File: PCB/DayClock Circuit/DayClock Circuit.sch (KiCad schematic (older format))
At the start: 28 parts, among them J10 Conn_02x08_Odd_Even, J11 Conn_01x02, J3 molex 15-24-4441, J5 4002 LCD Screen, J6 Encoder, J7 RGB_LED_Strip_Connector, J8 RGB_LED_Strip_Connector, J9 RGB_LED_Strip_Connector, Q1 N-MOSFET, Q2 N-MOSFET, Q3 N-MOSFET, Q4 N-MOSFET, Q5 N-MOSFET, Q6 N-MOSFET, Q7 N-MOSFET, Q8 N-MOSFET, Q9 N-MOSFET, U1 Tiny_RTC_DS1307

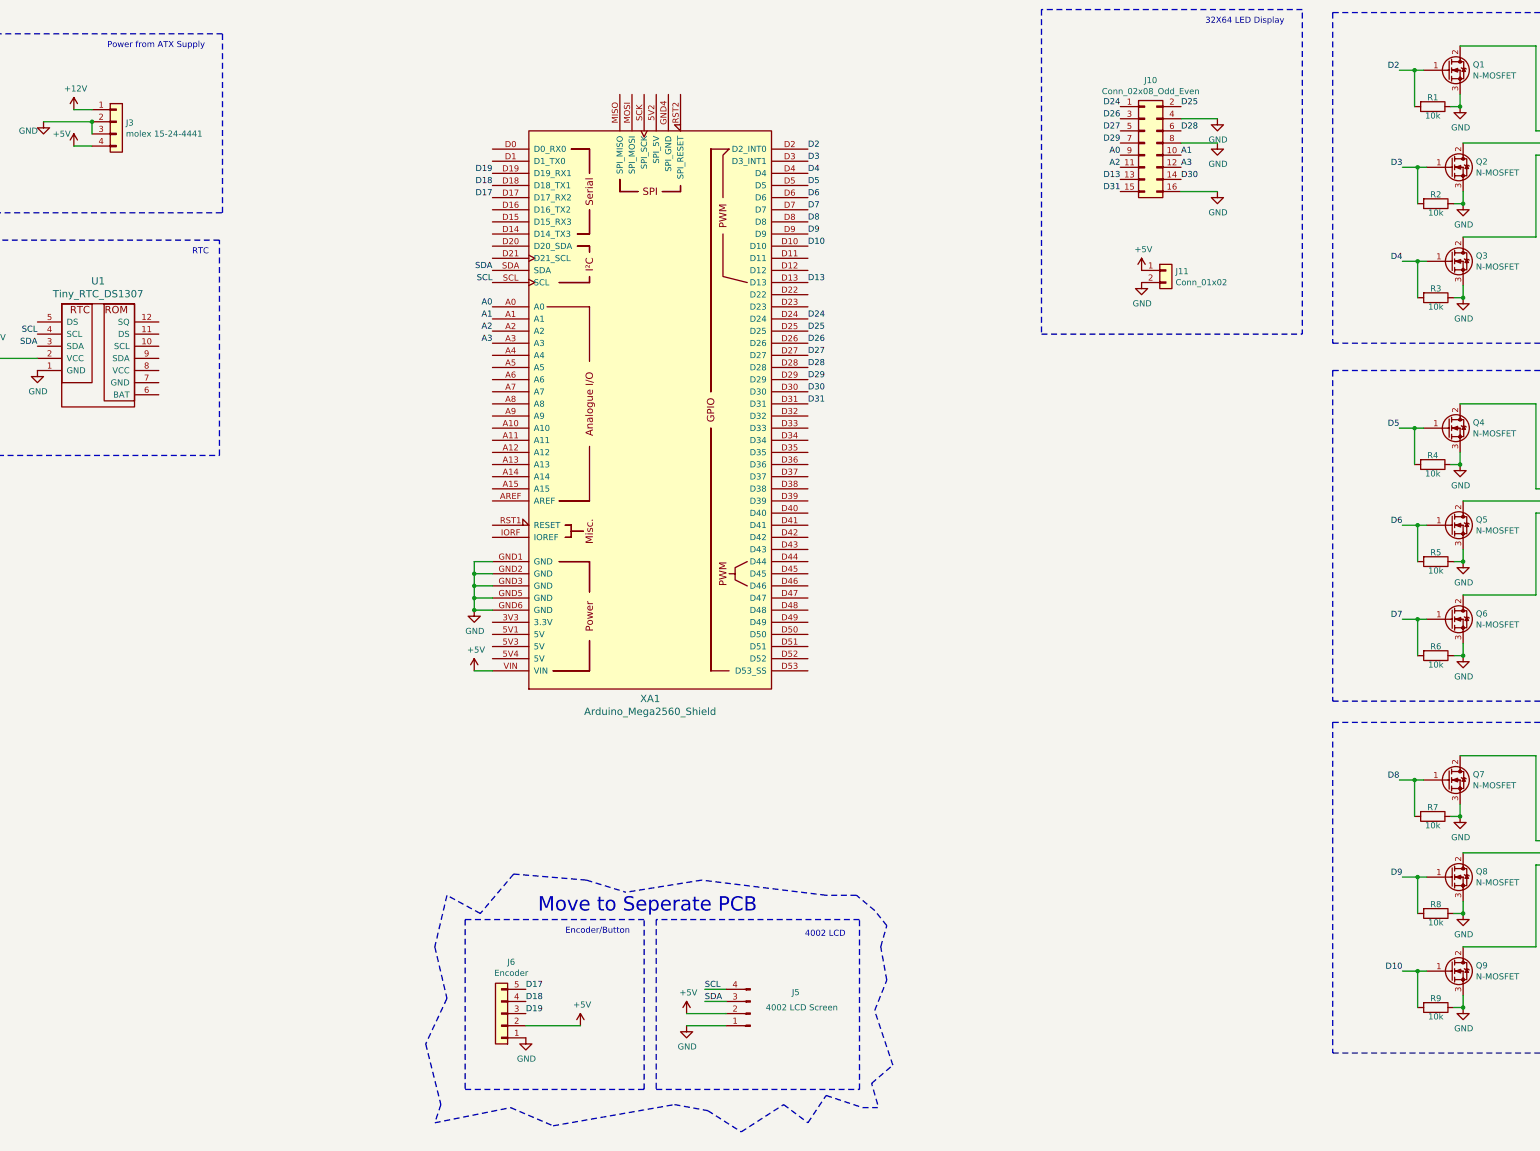
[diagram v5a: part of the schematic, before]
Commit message: Added Stepper with Driver and Proximity Sensor Limits
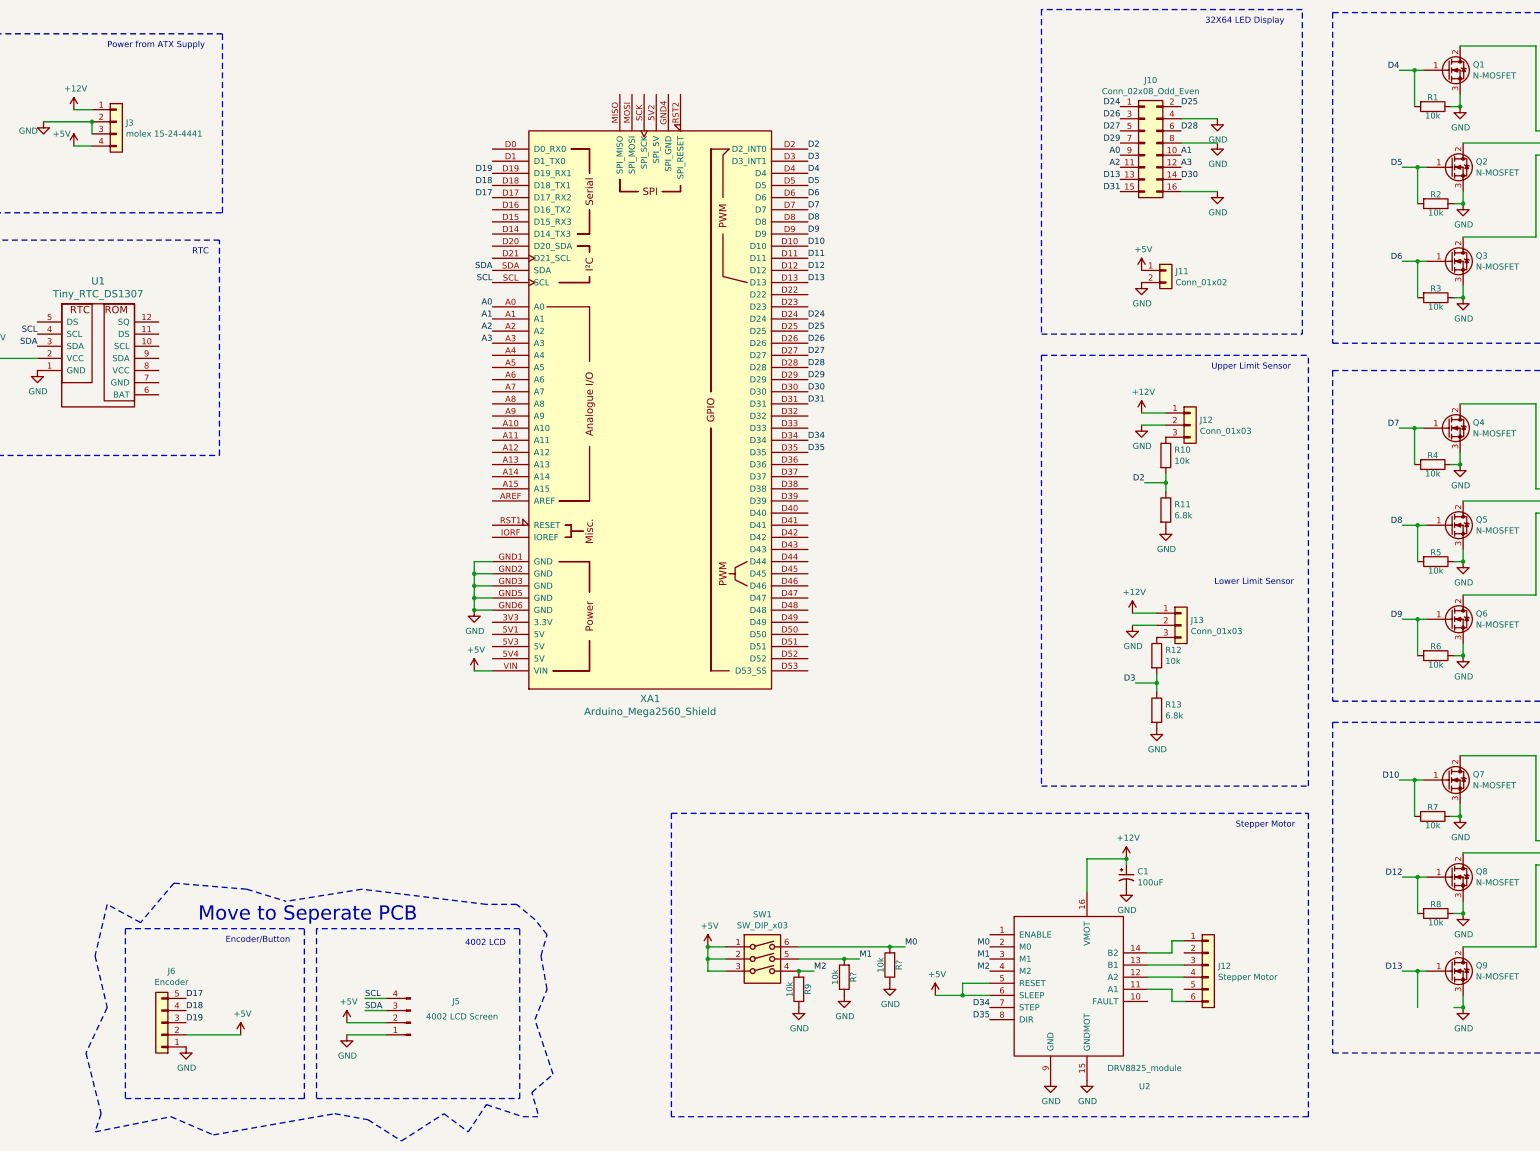
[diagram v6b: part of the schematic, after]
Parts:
- added C1: 100uF, symbol Device:CP1_Small
- added J12, J13: Conn_01x03, Connector_JST:JST_XH_B03B-XH-A_1x03_P2.50mm_Vertical, symbol Connector_Generic:Conn_01x03
- added J12: Stepper Motor, symbol Connector_Generic:Conn_01x06
- added R10, R12, R? (x2): 10k, Resistor_SMD:R_0805_2012Metric_Pad1.15x1.50mm_HandSolder, symbol Device:R
- added R11, R13: 6.8k, Resistor_SMD:R_0805_2012Metric_Pad1.15x1.50mm_HandSolder, symbol Device:R
- added SW1: SW_DIP_x03, symbol Switch:SW_DIP_x03
- added U2: DRV8825_module, symbol rich_symbols:DRV8825_module
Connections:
- net +12V: now also C1.1, J12.1 (Pin_1), J13.1 (Pin_1), U2.16 (VMOT)
- net +5V: now also SW1.1, SW1.2, SW1.3, U2.5 (RESET), U2.6 (SLEEP)
- net D10: now also Q7.1 (G), R7.2; no longer Q9.1 (G), R9.2
- net D13: now also Q9.1 (G)
- net D2: now also R10.2, R11.1; no longer Q1.1 (G), R1.2
- net D3: now also R12.2, R13.1; no longer Q2.1 (G), R2.2
- net D4: now also Q1.1 (G), R1.2; no longer Q3.1 (G), R3.2
- net D5: now also Q2.1 (G), R2.2; no longer Q4.1 (G), R4.2
- net D6: now also Q3.1 (G), R3.2; no longer Q5.1 (G), R5.2
- net D7: now also Q4.1 (G), R4.2; no longer Q6.1 (G), R6.2
- net D8: now also Q5.1 (G), R5.2; no longer Q7.1 (G), R7.2
- net D9: now also Q6.1 (G), R6.2; no longer Q8.1 (G), R8.2
- net GND: now also C1.2, J12.2 (Pin_2), J13.2 (Pin_2), R11.2, R13.2, R?.1, R?.1, U2.15 (GNDMOT), U2.9 (GND)
- net D11: now reaches XA1.D11
- net D12: now reaches XA1.D12
- net D12: now also Q8.1 (G), R8.2
- net D34: now reaches XA1.D34
- net D34: now also U2.7 (STEP)
- net D35: now reaches XA1.D35
- net D35: now also U2.8 (DIR)
- new net: J12.3 (Pin_3), R10.1
- new net: J13.3 (Pin_3), R12.1
- new net: J12.6 (Pin_6), U2.11 (A1)
- new net: J12.4 (Pin_4), U2.12 (A2)
- new net: J12.3 (Pin_3), U2.13 (B1)
- new net: J12.1 (Pin_1), U2.14 (B2)
- new net M0: R?.2, SW1.6, U2.2 (M0)
- new net M1: R?.2, SW1.5, U2.3 (M1)
- new net M2: R9.2, SW1.4, U2.4 (M2)
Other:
- note added: "Lower Limit Sensor"
- note added: "Stepper Motor"
- note added: "Upper Limit Sensor"
- moved on the sheet: J5, J6, R9

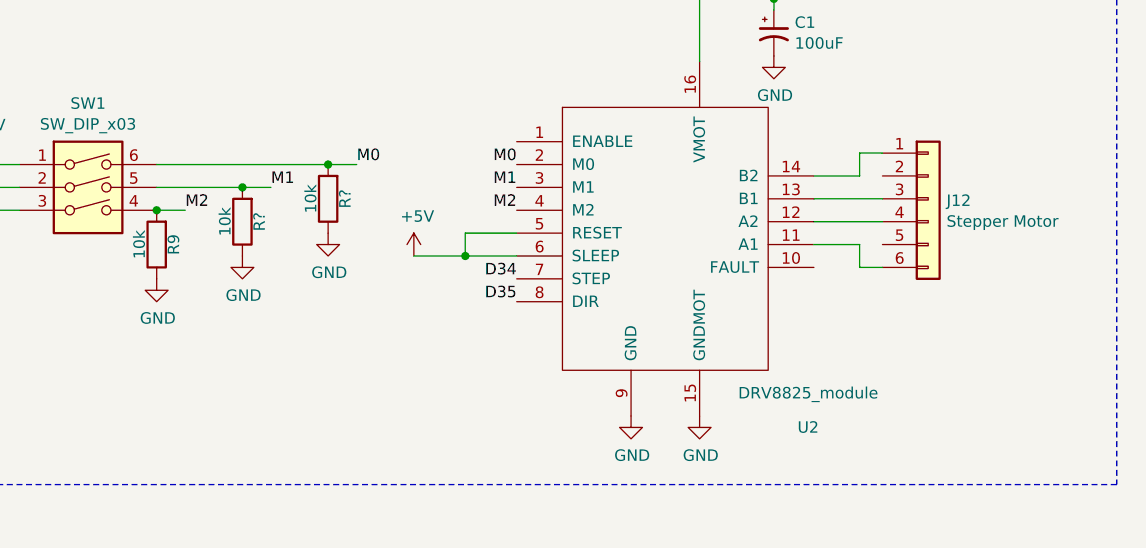
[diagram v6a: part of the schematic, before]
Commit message: Added resistors to steper sriver signal lines.  This solved somem erratic behaviour of the stpper moving on it's own
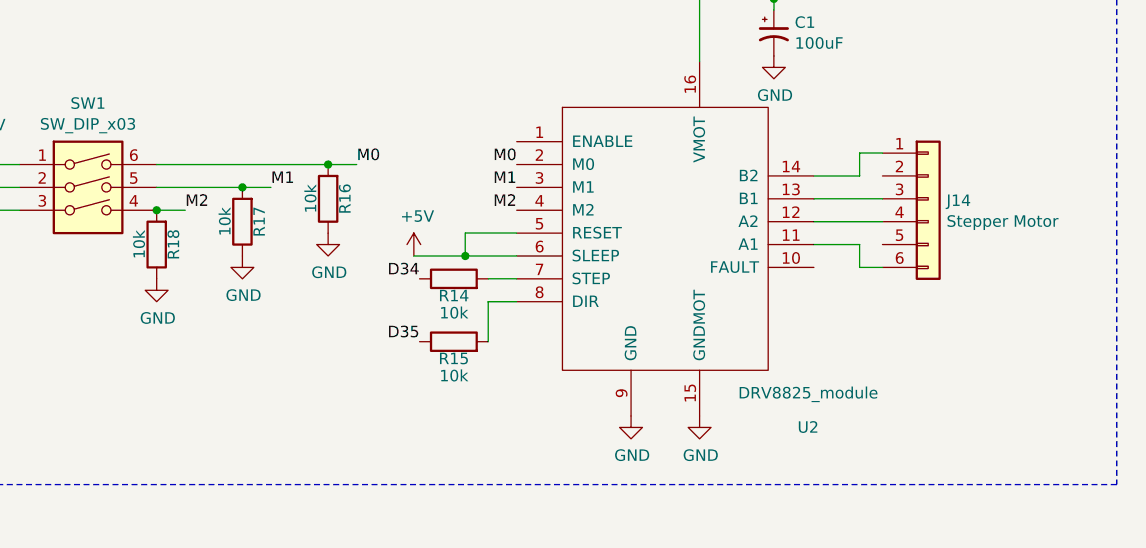
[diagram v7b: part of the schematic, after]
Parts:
- added R14, R15: 10k, Resistor_SMD:R_0805_2012Metric_Pad1.15x1.50mm_HandSolder, symbol Device:R
- gave numbers to parts that had none: 2
- renumbered J12 to J14, R9 to R18
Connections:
- net D34: now also R14.1; no longer U2.7 (STEP)
- net D35: now also R15.1; no longer U2.8 (DIR)
- new net: R15.2, U2.8 (DIR)
- new net: R14.2, U2.7 (STEP)
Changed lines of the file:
@@
 $EndComp
 $Comp
-L Connector_Generic:Conn_01x06 J12
+L Connector_Generic:Conn_01x06 J14
 U 1 1 5B169A57
 P 11500 8575
-F 0 "J12" H 11580 8567 50  0000 L CNN
+F 0 "J14" H 11580 8567 50  0000 L CNN
 F 1 "Stepper Motor" H 11580 8476 50  0000 L CNN
 F 2 "" H 11500 8575 50  0001 C CNN
@@
 $EndComp
 $Comp
-L power:GND #PWR?
+L power:GND #PWR0134
 U 1 1 5B17B857
 P 10825 7950
-F 0 "#PWR?" H 10825 7700 50  0001 C CNN
+F 0 "#PWR0134" H 10825 7700 50  0001 C CNN
 F 1 "GND" H 10830 7777 50  0000 C CNN
 F 2 "" H 10825 7950 50  0001 C CNN
@@
 	10825 7700 10825 7750
 $Comp
-L power:+12V #PWR?
+L power:+12V #PWR0135
 U 1 1 5B180478
 P 10825 7700
-F 0 "#PWR?" H 10825 7550 50  0001 C CNN
+F 0 "#PWR0135" H 10825 7550 50  0001 C CNN
 F 1 "+12V" H 10840 7873 50  0000 C CNN
 F 2 "" H 10825 7700 50  0001 C CNN
@@
 Connection ~ 10825 7700
 $Comp
-L power:+5V #PWR?
+L power:+5V #PWR0136
 U 1 1 5B180805
 P 9250 8825
-F 0 "#PWR?" H 9250 8675 50  0001 C CNN
+F 0 "#PWR0136" H 9250 8675 50  0001 C CNN
 F 1 "+5V" H 9265 8998 50  0000 C CNN
 F 2 "" H 9250 8825 50  0001 C CNN
@@
 	1    0    0    -1
 $EndComp
-Text Label 9700 8925 2    50   ~ 0
+Text Label 9275 8925 2    50   ~ 0
 D34
-Text Label 9700 9025 2    50   ~ 0
+Text Label 9275 9200 2    50   ~ 0
 D35
 Text Label 8200 4250 0    50   ~ 0
@@
 	9475 8725 9475 8825
 $Comp
-L power:+5V #PWR?
+L power:+5V #PWR0137
 U 1 1 5B1BE31D
 P 7375 8425
-F 0 "#PWR?" H 7375 8275 50  0001 C CNN
+F 0 "#PWR0137" H 7375 8275 50  0001 C CNN
 F 1 "+5V" H 7390 8598 50  0000 C CNN
 F 2 "" H 7375 8425 50  0001 C CNN
@@
 Connection ~ 9475 8825
 $Comp
-L Device:R R?
+L Device:R R16
 U 1 1 5B212CFE
 P 8875 8575
-F 0 "R?" V 8800 8575 50  0000 C CNN
+F 0 "R16" V 8800 8575 50  0000 C CNN
 F 1 "10k" V 8950 8575 50  0000 C CNN
 F 2 "Resistor_SMD:R_0805_2012Metric_Pad1.15x1.50mm_HandSolder" V 8805 8575 50  0001 C CNN
@@
 $EndComp
 $Comp
-L power:GND #PWR?
+L power:GND #PWR0138
 U 1 1 5B212D05
 P 8875 8725
-F 0 "#PWR?" H 8875 8475 50  0001 C CNN
+F 0 "#PWR0138" H 8875 8475 50  0001 C CNN
 F 1 "GND" H 8880 8552 50  0000 C CNN
 F 2 "" H 8875 8725 50  0001 C CNN
@@
 M1
 $Comp
-L power:GND #PWR?
+L power:GND #PWR0139
 U 1 1 5B20D121
 P 8500 8825
-F 0 "#PWR?" H 8500 8575 50  0001 C CNN
+F 0 "#PWR0139" H 8500 8575 50  0001 C CNN
 F 1 "GND" H 8505 8652 50  0000 C CNN
 F 2 "" H 8500 8825 50  0001 C CNN
@@
 Connection ~ 8500 8525
 $Comp
-L Device:R R?
+L Device:R R17
 U 1 1 5B20D11A
 P 8500 8675
-F 0 "R?" V 8425 8675 50  0000 C CNN
+F 0 "R17" V 8425 8675 50  0000 C CNN
 F 1 "10k" V 8575 8675 50  0000 C CNN
 F 2 "Resistor_SMD:R_0805_2012Metric_Pad1.15x1.50mm_HandSolder" V 8430 8675 50  0001 C CNN
@@
 M2
 $Comp
-L power:GND #PWR?
+L power:GND #PWR0140
 U 1 1 5B1F6902
 P 8125 8925
-F 0 "#PWR?" H 8125 8675 50  0001 C CNN
+F 0 "#PWR0140" H 8125 8675 50  0001 C CNN
 F 1 "GND" H 8130 8752 50  0000 C CNN
 F 2 "" H 8125 8925 50  0001 C CNN
@@
 Connection ~ 8125 8625
 $Comp
-L Device:R R9
+L Device:R R18
 U 1 1 5B0C69E9
 P 8125 8775
-F 0 "R9" V 8050 8775 50  0000 C CNN
+F 0 "R18" V 8050 8775 50  0000 C CNN
 F 1 "10k" V 8200 8775 50  0000 C CNN
 F 2 "Resistor_SMD:R_0805_2012Metric_Pad1.15x1.50mm_HandSolder" V 8055 8775 50  0001 C CNN
@@
 Text Notes 11725 7450 0    50   ~ 0
 Stepper Motor
+$Comp
+L Device:R R15
+U 1 1 5B11B9AE
+P 9425 9200
+F 0 "R15" V 9350 9200 50  0000 C CNN
+F 1 "10k" V 9275 9200 50  0000 C CNN
+F 2 "Resistor_SMD:R_0805_2012Metric_Pad1.15x1.50mm_HandSolder" V 9355 9200 50  0001 C CNN
+F 3 "~" H 9425 9200 50  0001 C CNN
+	1    9425 9200
+	0    -1   -1   0
+$EndComp
+Wire Wire Line
+	9575 8925 9700 8925
+$Comp
+L Device:R R14
+U 1 1 5B13A991
+P 9425 8925
+F 0 "R14" V 9350 8925 50  0000 C CNN
+F 1 "10k" V 9275 8925 50  0000 C CNN
+F 2 "Resistor_SMD:R_0805_2012Metric_Pad1.15x1.50mm_HandSolder" V 9355 8925 50  0001 C CNN
+F 3 "~" H 9425 8925 50  0001 C CNN
+	1    9425 8925
+	0    -1   -1   0
+$EndComp
+Wire Wire Line
+	9700 9025 9575 9025
+Wire Wire Line
+	9575 9025 9575 9200
 $EndSCHEMATC
